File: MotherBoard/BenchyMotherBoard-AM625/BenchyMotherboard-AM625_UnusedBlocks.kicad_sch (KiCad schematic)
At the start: 2 parts, among them U1 AM6254ATCGGAALW, U13 SII9022ACNU

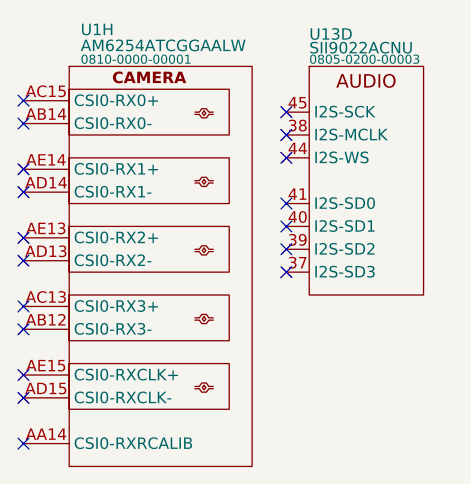
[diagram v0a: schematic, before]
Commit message: Schematic capture mostly complete. Starting PCB layout
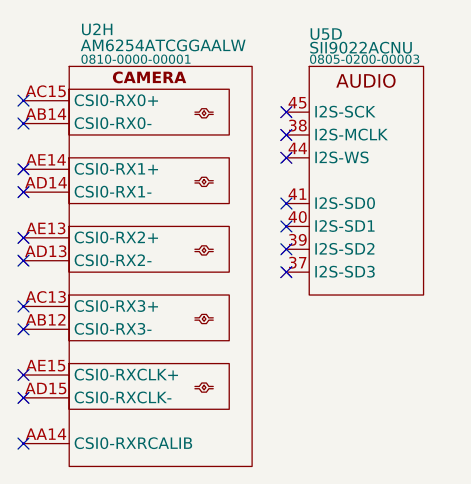
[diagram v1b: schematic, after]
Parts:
- renumbered U1 to U2, U13 to U5
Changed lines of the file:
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@@
 		(on_board yes)
 		(dnp no)
-		(property "Reference" "U1"
+		(property "Reference" "U2"
 			(at 20.32 13.716 0)
 			(effects
@@
 			(project "BenchyMotherBoard-AM625"
 				(path "/7184a1e6-58da-49c8-8a6c-ea31385ec956/7a96fb26-9078-4225-b61e-0daf3192c05c"
-					(reference "U1")
+					(reference "U2")
 					(unit 8)
 				)
@@
 		(on_board yes)
 		(dnp no)
-		(property "Reference" "U13"
+		(property "Reference" "U5"
 			(at 45.72 14.224 0)
 			(effects
@@
 			(project "BenchyMotherBoard-AM625"
 				(path "/7184a1e6-58da-49c8-8a6c-ea31385ec956/7a96fb26-9078-4225-b61e-0daf3192c05c"
-					(reference "U13")
+					(reference "U5")
 					(unit 4)
 				)
